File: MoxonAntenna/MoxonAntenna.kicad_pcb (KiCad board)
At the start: 2 copper layers, 222.4 x 88.4 mm, 6 parts

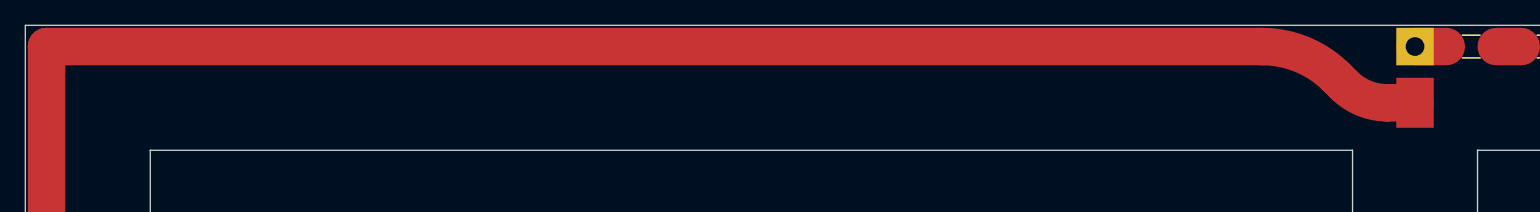
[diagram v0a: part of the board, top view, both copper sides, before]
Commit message: Updated PCB components
Found in stock components and put onto the PCB. Need to double check against datasheet to ensure all connections are good
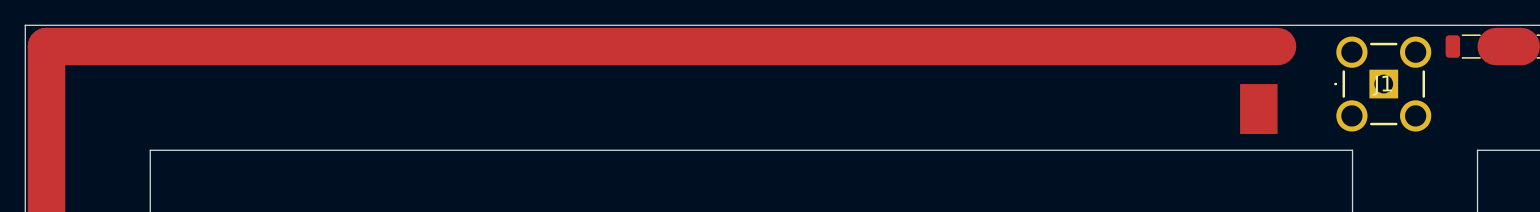
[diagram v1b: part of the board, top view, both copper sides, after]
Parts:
- removed the REF** at (159.5, 50.0)
- added J1: SMA_CONNECTOR, SamacSys_Parts:SMACONNECTOR, F.Cu at (157.0, 53.0)
- moved REF** 12.5 mm to (147.0, 55.0)
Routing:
- net Reflector: track 33.0 -> 0.00 mm
- net (no net): track 0.00 -> 33.0 mm
- net Shield: track 143.7 -> 131.5 mm
- net CenterA: track 2.50 -> 0.00 mm
